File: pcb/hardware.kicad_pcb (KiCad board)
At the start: 4 copper layers, 166 parts, among them J1 Micro_SD_Card_Det_Hirose_DM3AT, J2 USB_A, J3 USB_A, U1 AS4C512M16D3L-12BIN, U2 A33, U3 TPS62095RGTR, U4 TPS62095RGTR, U5 TPS62095RGTR, U6 TPS62095RGTR, U7 AP131-25, U8 MPM-15-5, Y1 24Mhz, Y2 32.768khz

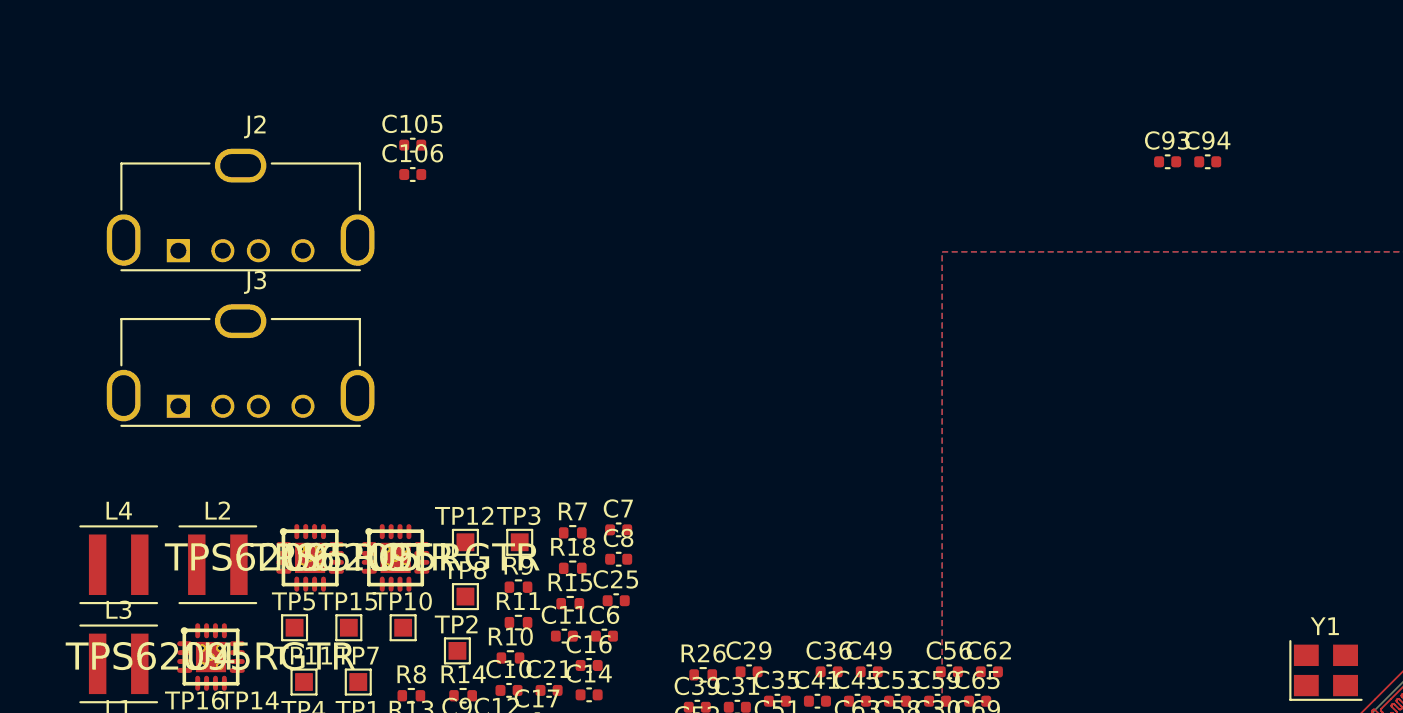
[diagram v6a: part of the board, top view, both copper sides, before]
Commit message: Added in the model for the 2x USB's
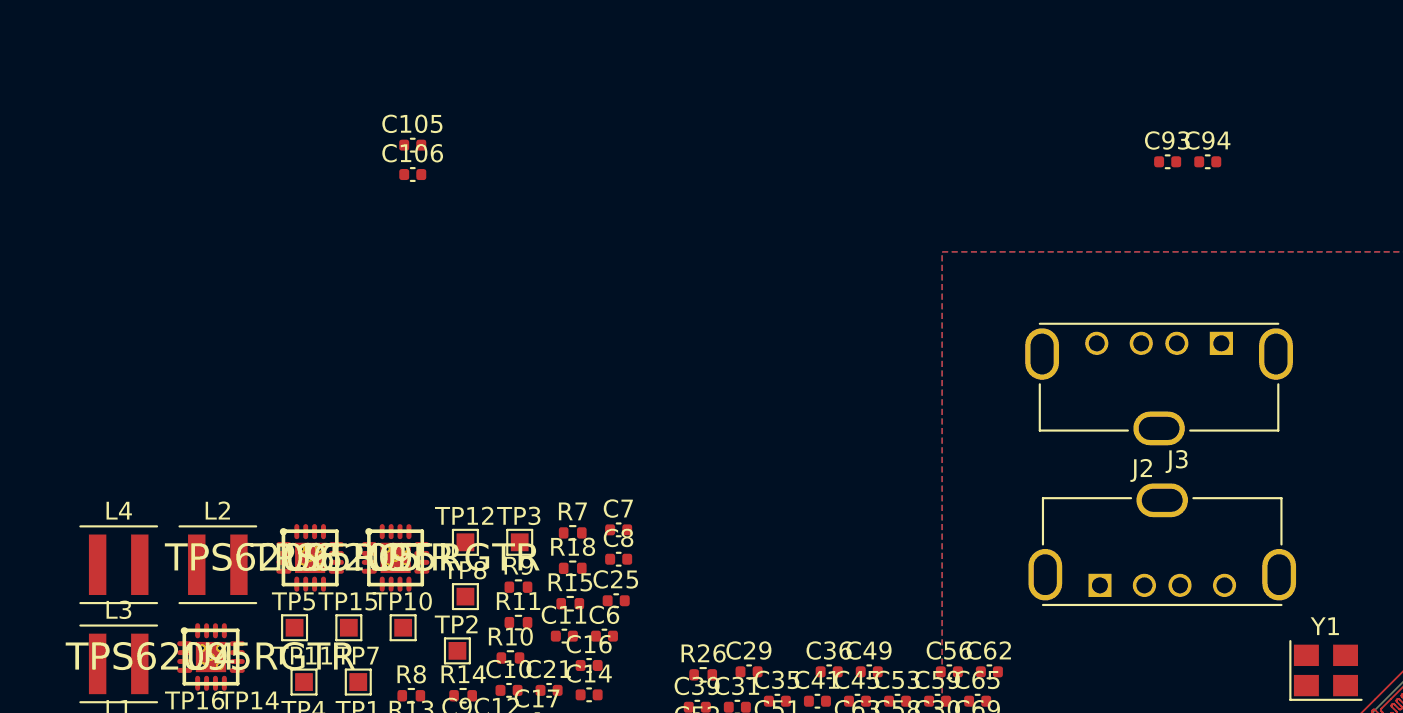
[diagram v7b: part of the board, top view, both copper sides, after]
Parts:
- moved J2 58.8 mm to (112.2, 80.0), turned to 180 degrees
- moved J3 52.7 mm to (105.3, 93.6)
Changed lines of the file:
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@@
     (45 Margin user)
     (46 B.CrtYd user hide)
-    (47 F.CrtYd user hide)
+    (47 F.CrtYd user)
     (48 B.Fab user hide)
     (49 F.Fab user hide)
@@
     (uvia_drill 0.6)
   )
+  (module Connector_USB:USB_A_Molex_105057_Vertical (layer F.Cu)
+    (at 105.3338 93.61932)
+    (descr https://www.molex.com/pdm_docs/sd/1050570001_sd.pdf)
+    (tags "USB A Vertical")
+    (fp_text reference J3 (at 4.4 -7.05) (layer F.SilkS)
+      (effects (font (size 1 1) (thickness 0.15)))
+    )
+    (fp_text value USB_A (at 3.5 2.4) (layer F.Fab)
+      (effects (font (size 1 1) (thickness 0.15)))
+    )
+    (fp_text user %R (at 3.45 -2.15) (layer F.Fab)
+      (effects (font (size 1 1) (thickness 0.15)))
+    )
+    (fp_line (start -3.05 -4.76) (end 10.05 -4.76) (layer F.Fab) (width 0.1))
+    (fp_line (start 10.05 -4.76) (end 10.05 0.96) (layer F.Fab) (width 0.1))
+    (fp_line (start -3.05 0.96) (end -3.05 -4.76) (layer F.Fab) (width 0.1))
+    (fp_line (start 11.52 -6.23) (end 11.52 1.46) (layer F.CrtYd) (width 0.05))
+    (fp_line (start 11.52 1.46) (end -4.52 1.46) (layer F.CrtYd) (width 0.05))
+    (fp_line (start -4.52 1.46) (end -4.52 -6.23) (layer F.CrtYd) (width 0.05))
+    (fp_line (start -4.52 -6.23) (end 11.52 -6.23) (layer F.CrtYd) (width 0.05))
+    (fp_line (start -0.65 0.96) (end 0 0.2) (layer F.Fab) (width 0.1))
+    (fp_line (start 0 0.2) (end 0.65 0.96) (layer F.Fab) (width 0.1))
+    (fp_line (start -0.65 0.96) (end -3.05 0.96) (layer F.Fab) (width 0.1))
+    (fp_line (start 10.05 0.96) (end 0.65 0.96) (layer F.Fab) (width 0.1))
+    (fp_line (start -3.2 -4.9) (end 1.75 -4.9) (layer F.SilkS) (width 0.12))
+    (fp_line (start -3.2 -4.9) (end -3.2 -2.3) (layer F.SilkS) (width 0.12))
+    (fp_line (start 10.2 -4.9) (end 10.2 -2.3) (layer F.SilkS) (width 0.12))
+    (fp_line (start 10.2 -4.9) (end 5.25 -4.9) (layer F.SilkS) (width 0.12))
+    (fp_line (start 10.2 1.1) (end -3.2 1.1) (layer F.SilkS) (width 0.12))
+    (pad 5 thru_hole oval (at 3.5 -4.78 90) (size 1.9 2.9) (drill oval 1.3 2.3) (layers *.Cu *.Mask)
+      (net 169 GND))
+    (pad 5 thru_hole oval (at 10.07 -0.6) (size 1.9 2.9) (drill oval 1.3 2.3) (layers *.Cu *.Mask)
+      (net 169 GND))
+    (pad 5 thru_hole oval (at -3.07 -0.6 180) (size 1.9 2.9) (drill oval 1.3 2.3) (layers *.Cu *.Mask)
+      (net 169 GND))
+    (pad 4 thru_hole circle (at 7 0) (size 1.3 1.3) (drill 0.9) (layers *.Cu *.Mask)
+      (net 169 GND))
+    (pad 3 thru_hole circle (at 4.5 0) (size 1.3 1.3) (drill 0.9) (layers *.Cu *.Mask)
+      (net 252 "Net-(J3-Pad3)"))
+    (pad 2 thru_hole circle (at 2.5 0) (size 1.3 1.3) (drill 0.9) (layers *.Cu *.Mask)
+      (net 253 "Net-(J3-Pad2)"))
+    (pad 1 thru_hole rect (at 0 0) (size 1.3 1.3) (drill 0.9) (layers *.Cu *.Mask)
+      (net 196 +5V))
+    (model ${KIPRJMOD}/1050570001/1050570001.stp
+      (offset (xyz 3.2 2 5.5))
+      (scale (xyz 1 1 1))
+      (rotate (xyz 0 0 0))
+    )
+  )
   (module AS4C512M16D3L:Alliance_Memory-AS4C512M16D3L-12BIN-0-0-IPC_A (layer F.Cu)
     (at 135.5532 100.8632 90)
@@
     (pad A1 smd circle (at -3.2 -6 90) (size 0.3995 0.3995) (layers F.Cu F.Paste F.Mask)
       (net 168 +1V35))
-    (model eec.models/Alliance_Memory_-_AS4C512M16D3L-12BIN.step
-      (offset (xyz -326.9513858896827 3.065068753967285 16.95493154536247))
+    (model ${KIPRJMOD}/AS4C512M16D3L/eec.models/Alliance_Memory_-_AS4C512M16D3L-12BIN.step
+      (offset (xyz -12.9 -0.1 0))
       (scale (xyz 1 1 1))
       (rotate (xyz -180 0 -180))
@@
   )
   (module Connector_USB:USB_A_Molex_105057_Vertical (layer F.Cu)
-    (at 53.5558 83.5548)
-    (descr https://www.molex.com/pdm_docs/sd/1050570001_sd.pdf)
-    (tags "USB A Vertical")
-    (fp_text reference J3 (at 4.4 -7.05) (layer F.SilkS)
-      (effects (font (size 1 1) (thickness 0.15)))
-    )
-    (fp_text value USB_A (at 3.5 2.4) (layer F.Fab)
-      (effects (font (size 1 1) (thickness 0.15)))
-    )
-    (fp_line (start -3.05 -4.76) (end 10.05 -4.76) (layer F.Fab) (width 0.1))
-    (fp_line (start 10.05 -4.76) (end 10.05 0.96) (layer F.Fab) (width 0.1))
-    (fp_line (start -3.05 0.96) (end -3.05 -4.76) (layer F.Fab) (width 0.1))
-    (fp_line (start 11.52 -6.23) (end 11.52 1.46) (layer F.CrtYd) (width 0.05))
-    (fp_line (start 11.52 1.46) (end -4.52 1.46) (layer F.CrtYd) (width 0.05))
-    (fp_line (start -4.52 1.46) (end -4.52 -6.23) (layer F.CrtYd) (width 0.05))
-    (fp_line (start -4.52 -6.23) (end 11.52 -6.23) (layer F.CrtYd) (width 0.05))
-    (fp_line (start -0.65 0.96) (end 0 0.2) (layer F.Fab) (width 0.1))
-    (fp_line (start 0 0.2) (end 0.65 0.96) (layer F.Fab) (width 0.1))
-    (fp_line (start -0.65 0.96) (end -3.05 0.96) (layer F.Fab) (width 0.1))
-    (fp_line (start 10.05 0.96) (end 0.65 0.96) (layer F.Fab) (width 0.1))
-    (fp_line (start -3.2 -4.9) (end 1.75 -4.9) (layer F.SilkS) (width 0.12))
-    (fp_line (start -3.2 -4.9) (end -3.2 -2.3) (layer F.SilkS) (width 0.12))
-    (fp_line (start 10.2 -4.9) (end 10.2 -2.3) (layer F.SilkS) (width 0.12))
-    (fp_line (start 10.2 -4.9) (end 5.25 -4.9) (layer F.SilkS) (width 0.12))
-    (fp_line (start 10.2 1.1) (end -3.2 1.1) (layer F.SilkS) (width 0.12))
-    (fp_text user %R (at 3.45 -2.15) (layer F.Fab)
-      (effects (font (size 1 1) (thickness 0.15)))
-    )
-    (pad 5 thru_hole oval (at 3.5 -4.78 90) (size 1.9 2.9) (drill oval 1.3 2.3) (layers *.Cu *.Mask)
-      (net 169 GND))
-    (pad 5 thru_hole oval (at 10.07 -0.6) (size 1.9 2.9) (drill oval 1.3 2.3) (layers *.Cu *.Mask)
-      (net 169 GND))
-    (pad 5 thru_hole oval (at -3.07 -0.6 180) (size 1.9 2.9) (drill oval 1.3 2.3) (layers *.Cu *.Mask)
-      (net 169 GND))
-    (pad 4 thru_hole circle (at 7 0) (size 1.3 1.3) (drill 0.9) (layers *.Cu *.Mask)
-      (net 169 GND))
-    (pad 3 thru_hole circle (at 4.5 0) (size 1.3 1.3) (drill 0.9) (layers *.Cu *.Mask)
-      (net 252 "Net-(J3-Pad3)"))
-    (pad 2 thru_hole circle (at 2.5 0) (size 1.3 1.3) (drill 0.9) (layers *.Cu *.Mask)
-      (net 253 "Net-(J3-Pad2)"))
-    (pad 1 thru_hole rect (at 0 0) (size 1.3 1.3) (drill 0.9) (layers *.Cu *.Mask)
-      (net 196 +5V))
-    (model ${KISYS3DMOD}/Connector_USB.3dshapes/USB_A_Molex_105057_Vertical.wrl
-      (at (xyz 0 0 0))
-      (scale (xyz 1 1 1))
-      (rotate (xyz 0 0 0))
-    )
-  )
-  (module Connector_USB:USB_A_Molex_105057_Vertical (layer F.Cu)
-    (at 53.5558 74.8148)
+    (at 112.15624 80.02016 180)
     (descr https://www.molex.com/pdm_docs/sd/1050570001_sd.pdf)
     (tags "USB A Vertical")
@@
       (effects (font (size 1 1) (thickness 0.15)))
     )
-    (pad 5 thru_hole oval (at 3.5 -4.78 90) (size 1.9 2.9) (drill oval 1.3 2.3) (layers *.Cu *.Mask)
+    (pad 5 thru_hole oval (at 3.5 -4.78 270) (size 1.9 2.9) (drill oval 1.3 2.3) (layers *.Cu *.Mask)
       (net 169 GND))
-    (pad 5 thru_hole oval (at 10.07 -0.6) (size 1.9 2.9) (drill oval 1.3 2.3) (layers *.Cu *.Mask)
+    (pad 5 thru_hole oval (at 10.07 -0.6 180) (size 1.9 2.9) (drill oval 1.3 2.3) (layers *.Cu *.Mask)
       (net 169 GND))
-    (pad 5 thru_hole oval (at -3.07 -0.6 180) (size 1.9 2.9) (drill oval 1.3 2.3) (layers *.Cu *.Mask)
+    (pad 5 thru_hole oval (at -3.07 -0.6) (size 1.9 2.9) (drill oval 1.3 2.3) (layers *.Cu *.Mask)
       (net 169 GND))
-    (pad 4 thru_hole circle (at 7 0) (size 1.3 1.3) (drill 0.9) (layers *.Cu *.Mask)
+    (pad 4 thru_hole circle (at 7 0 180) (size 1.3 1.3) (drill 0.9) (layers *.Cu *.Mask)
       (net 169 GND))
-    (pad 3 thru_hole circle (at 4.5 0) (size 1.3 1.3) (drill 0.9) (layers *.Cu *.Mask)
+    (pad 3 thru_hole circle (at 4.5 0 180) (size 1.3 1.3) (drill 0.9) (layers *.Cu *.Mask)
       (net 250 "Net-(J2-Pad3)"))
-    (pad 2 thru_hole circle (at 2.5 0) (size 1.3 1.3) (drill 0.9) (layers *.Cu *.Mask)
+    (pad 2 thru_hole circle (at 2.5 0 180) (size 1.3 1.3) (drill 0.9) (layers *.Cu *.Mask)
       (net 251 "Net-(J2-Pad2)"))
-    (pad 1 thru_hole rect (at 0 0) (size 1.3 1.3) (drill 0.9) (layers *.Cu *.Mask)
+    (pad 1 thru_hole rect (at 0 0 180) (size 1.3 1.3) (drill 0.9) (layers *.Cu *.Mask)
       (net 196 +5V))
-    (model ${KISYS3DMOD}/Connector_USB.3dshapes/USB_A_Molex_105057_Vertical.wrl
-      (at (xyz 0 0 0))
+    (model ${KIPRJMOD}/1050570001/1050570001.stp
+      (offset (xyz 3.5 2 5.5))
       (scale (xyz 1 1 1))
       (rotate (xyz 0 0 0))

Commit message: Working on the layout
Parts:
- removed TP19, TP4, TP7, TP8: TestPoint, TestPoint:TestPoint_Pad_1.0x1.0mm
- C40, C43, C48, C56, R20, R21, R22, R23, R24, R26, R6: moved to B.Cu
- moved C97 99.0 mm to (121.2, 97.5)
- moved C98 89.7 mm to (114.8, 99.2), turned to 180 degrees
- moved Y2 87.8 mm to (105.6, 103.8), turned to 90 degrees
- moved R30 87.0 mm to (102.4, 95.2)
- moved C96 85.3 mm to (105.6, 101.9), turned to 270 degrees
- moved C95 85.2 mm to (105.6, 105.8), turned to 90 degrees
- moved C102 76.8 mm to (106.4, 108.2), turned to 180 degrees
- moved R29 69.2 mm to (106.9, 103.8), turned to 90 degrees
- moved C41 68.1 mm to (105.4, 166.3)
- moved C45 68.1 mm to (107.7, 166.3)
- moved C53 68.1 mm to (109.9, 166.3)
- moved C49 68.1 mm to (108.3, 164.7)
- moved C62 65.9 mm to (109.3, 163.6)
- moved C31 64.5 mm to (103.3, 162.3)
- moved C33 64.5 mm to (101.0, 165.6)
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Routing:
- net Net-(R6-Pad1): track 0.00 -> 3.61 mm, vias 0 -> 1
- net +1V1: vias 0 -> 1
- added copper zone on F.Cu, net +1V1
